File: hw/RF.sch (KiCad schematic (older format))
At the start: 18 parts

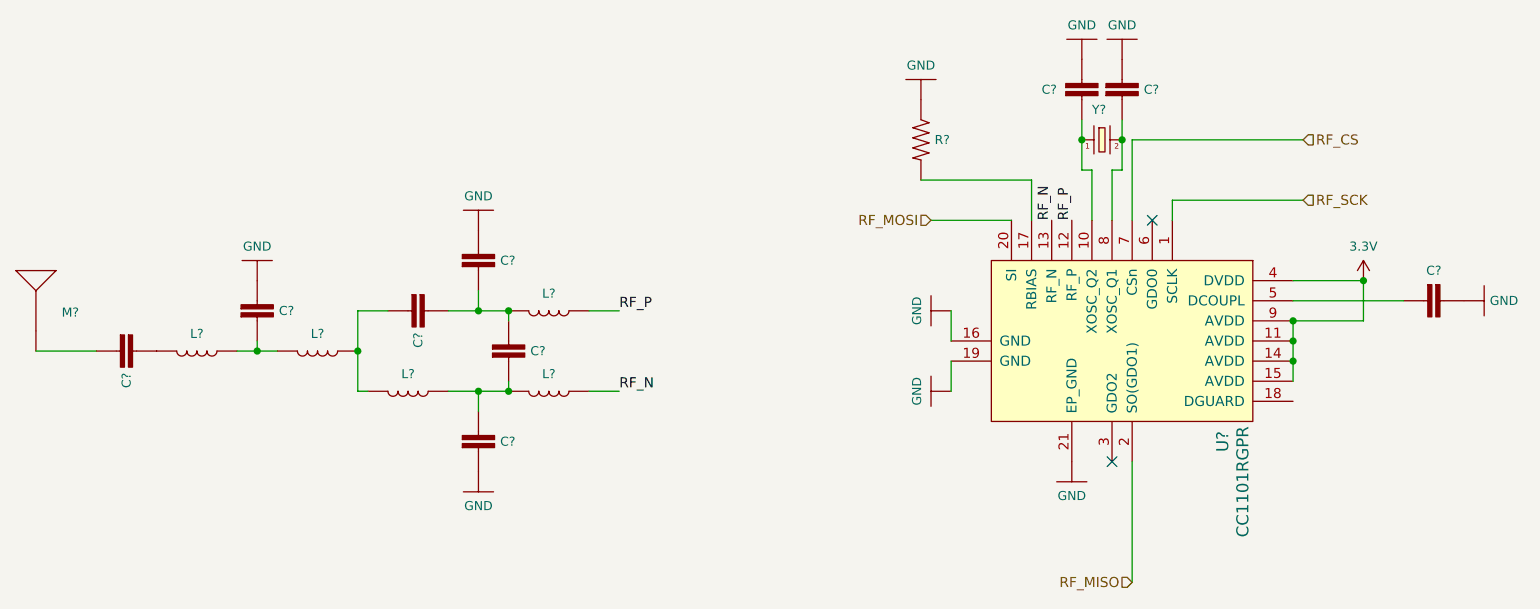
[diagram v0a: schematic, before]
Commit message: Create first revision of IMU sheet assign some footprints.
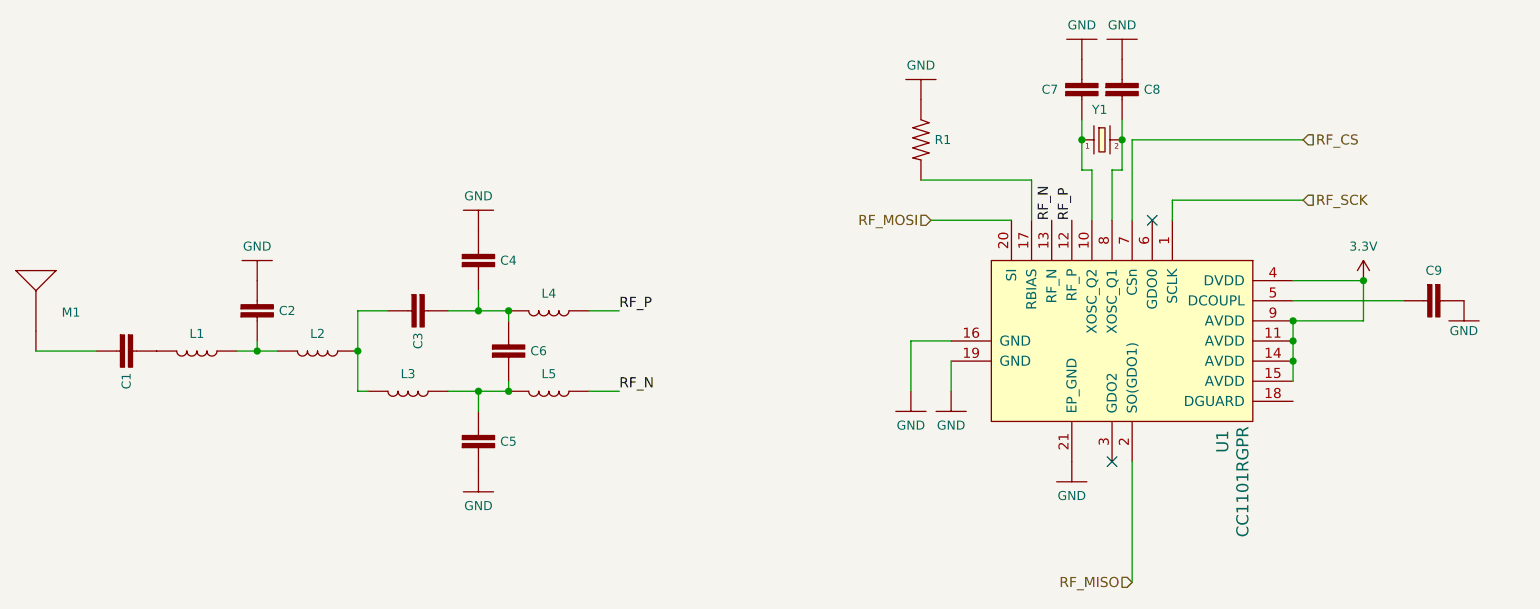
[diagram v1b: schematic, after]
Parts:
- gave numbers to parts that had none: 18
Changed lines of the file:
@@
 EESchema Schematic File Version 4
+LIBS:drone-cache
 EELAYER 30 0
 EELAYER END
 $Descr A 11000 8500
 encoding utf-8
-Sheet 2 2
+Sheet 2 3
 Title ""
 Date "2019-10-03"
@@
 $EndDescr
 $Comp
-L dk_RF-Transceiver-ICs:CC1101RGPR U?
+L dk_RF-Transceiver-ICs:CC1101RGPR U1
 U 1 1 5D96A68A
 P 7300 4000
-F 0 "U?" H 7800 4350 60  0000 C CNN
+F 0 "U1" H 7800 4350 60  0000 C CNN
 F 1 "CC1101RGPR" H 8000 4450 60  0000 C CNN
 F 2 "digikey-footprints:QFN-20-1EP_4x4mm_RevA" H 7500 4200 60  0001 L CNN
@@
 $EndComp
 $Comp
-L SparkFun-PowerSymbols:GND #GND?
+L SparkFun-PowerSymbols:GND #GND0101
 U 1 1 5D96E54E
 P 6300 4250
-F 0 "#GND?" H 6350 4200 45  0001 L BNN
+F 0 "#GND0101" H 6350 4200 45  0001 L BNN
 F 1 "GND" H 6300 4080 45  0000 C CNN
 F 2 "" H 6300 4150 60  0001 C CNN
 F 3 "" H 6300 4150 60  0001 C CNN
 	1    6300 4250
-	0    1    1    0
-$EndComp
-$Comp
-L SparkFun-PowerSymbols:GND #GND?
+	1    0    0    -1
+$EndComp
+$Comp
+L SparkFun-PowerSymbols:GND #GND0102
 U 1 1 5D96EA50
-P 6300 3850
-F 0 "#GND?" H 6350 3800 45  0001 L BNN
-F 1 "GND" H 6300 3680 45  0000 C CNN
-F 2 "" H 6300 3750 60  0001 C CNN
-F 3 "" H 6300 3750 60  0001 C CNN
-	1    6300 3850
-	0    1    1    0
+P 6100 4250
+F 0 "#GND0102" H 6150 4200 45  0001 L BNN
+F 1 "GND" H 6100 4080 45  0000 C CNN
+F 2 "" H 6100 4150 60  0001 C CNN
+F 3 "" H 6100 4150 60  0001 C CNN
+	1    6100 4250
+	1    0    0    -1
 $EndComp
 Wire Wire Line
 	6300 4100 6300 4250
-Wire Wire Line
-	6300 3850 6300 4000
-$Comp
-L SparkFun-Clocks:CRYSTALPTH-2X6 Y?
+$Comp
+L SparkFun-Clocks:CRYSTALPTH-2X6 Y1
 U 1 1 5D9752D5
 P 7050 3000
-F 0 "Y?" H 7000 3150 45  0000 L CNN
+F 0 "Y1" H 7000 3150 45  0000 L CNN
 F 1 "CRYSTALPTH-2X6" V 7050 2200 45  0001 L CNN
 F 2 "CRYSTAL-PTH-2X6-CYL" H 7050 3200 20  0001 C CNN
@@
 $EndComp
 $Comp
-L SparkFun-Capacitors:0.1UF-KIT-EZ-50V-20% C?
+L SparkFun-Capacitors:0.1UF-KIT-EZ-50V-20% C7
 U 1 1 5D981962
 P 6950 2800
-F 0 "C?" H 6750 2850 45  0000 L CNN
+F 0 "C7" H 6750 2850 45  0000 L CNN
 F 1 "0.1UF-KIT-EZ-50V-20%" H 7058 2861 45  0001 L CNN
 F 2 "CAP-PTH-SMALL-KIT" H 6950 3050 20  0001 C CNN
@@
 $EndComp
 $Comp
-L SparkFun-PowerSymbols:GND #GND?
+L SparkFun-PowerSymbols:GND #GND0103
 U 1 1 5D9935AD
 P 6950 2600
-F 0 "#GND?" H 7000 2550 45  0001 L BNN
+F 0 "#GND0103" H 7000 2550 45  0001 L BNN
 F 1 "GND" H 6950 2430 45  0000 C CNN
 F 2 "" H 6950 2500 60  0001 C CNN
@@
 Connection ~ 6950 3000
 $Comp
-L SparkFun-Capacitors:0.1UF-KIT-EZ-50V-20% C?
+L SparkFun-Capacitors:0.1UF-KIT-EZ-50V-20% C8
 U 1 1 5D9AA820
 P 7150 2800
-F 0 "C?" H 7258 2850 45  0000 L CNN
+F 0 "C8" H 7258 2850 45  0000 L CNN
 F 1 "0.1UF-KIT-EZ-50V-20%" H 7258 2861 45  0001 L CNN
 F 2 "CAP-PTH-SMALL-KIT" H 7150 3050 20  0001 C CNN
@@
 $EndComp
 $Comp
-L SparkFun-PowerSymbols:GND #GND?
+L SparkFun-PowerSymbols:GND #GND0104
 U 1 1 5D9AA826
 P 7150 2600
-F 0 "#GND?" H 7200 2550 45  0001 L BNN
+F 0 "#GND0104" H 7200 2550 45  0001 L BNN
 F 1 "GND" H 7150 2430 45  0000 C CNN
 F 2 "" H 7150 2500 60  0001 C CNN
@@
 Connection ~ 8000 4100
 $Comp
-L SparkFun-PowerSymbols:3.3V #SUPPLY?
+L SparkFun-PowerSymbols:3.3V #SUPPLY0101
 U 1 1 5D9B151B
 P 8350 3700
-F 0 "#SUPPLY?" H 8400 3700 45  0001 L BNN
+F 0 "#SUPPLY0101" H 8400 3700 45  0001 L BNN
 F 1 "3.3V" H 8350 3870 45  0000 C CNN
 F 2 "XXX-00000" H 8350 3881 60  0001 C CNN
@@
 RF_SCK
 $Comp
-L SparkFun-PowerSymbols:GND #GND?
+L SparkFun-PowerSymbols:GND #GND0105
 U 1 1 5D9B86E3
 P 6150 2800
-F 0 "#GND?" H 6200 2750 45  0001 L BNN
+F 0 "#GND0105" H 6200 2750 45  0001 L BNN
 F 1 "GND" H 6150 2630 45  0000 C CNN
 F 2 "" H 6150 2700 60  0001 C CNN
@@
 $EndComp
 $Comp
-L SparkFun-Resistors:RESISTOR0402 R?
+L SparkFun-Resistors:RESISTOR0402 R1
 U 1 1 5D9B8F7F
 P 6150 3000
-F 0 "R?" V 6150 3068 45  0000 L CNN
+F 0 "R1" V 6150 3068 45  0000 L CNN
 F 1 "RESISTOR0402" V 6139 3068 45  0001 L CNN
 F 2 "0402" H 6150 3150 20  0001 C CNN
@@
 	7200 4600 7200 5200
 $Comp
-L SparkFun-PowerSymbols:GND #GND?
+L SparkFun-PowerSymbols:GND #GND0106
 U 1 1 5D9F85B8
 P 6900 4600
-F 0 "#GND?" H 6950 4550 45  0001 L BNN
+F 0 "#GND0106" H 6950 4550 45  0001 L BNN
 F 1 "GND" H 6900 4430 45  0000 C CNN
 F 2 "" H 6900 4500 60  0001 C CNN
@@
 $EndComp
 $Comp
-L SparkFun-Capacitors:0.1UF-KIT-EZ-50V-20% C?
+L SparkFun-Capacitors:0.1UF-KIT-EZ-50V-20% C9
 U 1 1 5DA0075A
 P 8650 3800
-F 0 "C?" V 8500 3850 45  0000 C CNN
+F 0 "C9" V 8500 3850 45  0000 C CNN
 F 1 "0.1UF-KIT-EZ-50V-20%" H 8758 3861 45  0001 L CNN
 F 2 "CAP-PTH-SMALL-KIT" H 8650 4050 20  0001 C CNN
@@
 	8000 3800 8550 3800
 $Comp
-L SparkFun-PowerSymbols:GND #GND?
+L SparkFun-PowerSymbols:GND #GND0107
 U 1 1 5DA01234
 P 8850 3800
-F 0 "#GND?" H 8900 3750 45  0001 L BNN
-F 1 "GND" V 8850 3672 45  0000 R CNN
+F 0 "#GND0107" H 8900 3750 45  0001 L BNN
+F 1 "GND" H 8920 3650 45  0000 R CNN
 F 2 "" H 8850 3700 60  0001 C CNN
 F 3 "" H 8850 3700 60  0001 C CNN
 	1    8850 3800
-	0    -1   -1   0
+	1    0    0    -1
 $EndComp
 Text Label 6800 3400 1    50   ~ 0
@@
 RF_P
 $Comp
-L SparkFun-Coils:INDUCTOR-0402-3.9NH L?
+L SparkFun-Coils:INDUCTOR-0402-3.9NH L5
 U 1 1 5DA164EE
 P 4300 4250
-F 0 "L?" V 4214 4250 45  0000 C CNN
+F 0 "L5" V 4214 4250 45  0000 C CNN
 F 1 "INDUCTOR-0402-3.9NH" V 4108 4250 45  0001 C CNN
 F 2 "0402" H 4300 4500 20  0001 C CNN
@@
 $EndComp
 $Comp
-L SparkFun-Coils:INDUCTOR-0402-3.9NH L?
+L SparkFun-Coils:INDUCTOR-0402-3.9NH L4
 U 1 1 5DA177FA
 P 4300 3850
-F 0 "L?" V 4214 3850 45  0000 C CNN
+F 0 "L4" V 4214 3850 45  0000 C CNN
 F 1 "INDUCTOR-0402-3.9NH" V 4108 3850 45  0001 C CNN
 F 2 "0402" H 4300 4100 20  0001 C CNN
@@
 $EndComp
 $Comp
-L SparkFun-Coils:INDUCTOR-0402-3.9NH L?
+L SparkFun-Coils:INDUCTOR-0402-3.9NH L3
 U 1 1 5DA17EF8
 P 3600 4250
-F 0 "L?" V 3514 4250 45  0000 C CNN
+F 0 "L3" V 3514 4250 45  0000 C CNN
 F 1 "INDUCTOR-0402-3.9NH" V 3408 4250 45  0001 C CNN
 F 2 "0402" H 3600 4500 20  0001 C CNN
@@
 $EndComp
 $Comp
-L SparkFun-Capacitors:0.1UF-KIT-EZ-50V-20% C?
+L SparkFun-Capacitors:0.1UF-KIT-EZ-50V-20% C6
 U 1 1 5DA1B017
 P 4100 4100
-F 0 "C?" H 4208 4150 45  0000 L CNN
+F 0 "C6" H 4208 4150 45  0000 L CNN
 F 1 "0.1UF-KIT-EZ-50V-20%" H 4208 4161 45  0001 L CNN
 F 2 "CAP-PTH-SMALL-KIT" H 4100 4350 20  0001 C CNN
@@
 $EndComp
 $Comp
-L SparkFun-Capacitors:0.1UF-KIT-EZ-50V-20% C?
+L SparkFun-Capacitors:0.1UF-KIT-EZ-50V-20% C3
 U 1 1 5DA1BF75
 P 3600 3850
-F 0 "C?" H 3708 3900 45  0000 L CNN
+F 0 "C3" H 3708 3900 45  0000 L CNN
 F 1 "0.1UF-KIT-EZ-50V-20%" H 3708 3911 45  0001 L CNN
 F 2 "CAP-PTH-SMALL-KIT" H 3600 4100 20  0001 C CNN
@@
 $EndComp
 $Comp
-L SparkFun-Capacitors:0.1UF-KIT-EZ-50V-20% C?
+L SparkFun-Capacitors:0.1UF-KIT-EZ-50V-20% C4
 U 1 1 5DA21E27
 P 3950 3650
-F 0 "C?" H 4058 3700 45  0000 L CNN
+F 0 "C4" H 4058 3700 45  0000 L CNN
 F 1 "0.1UF-KIT-EZ-50V-20%" H 4058 3711 45  0001 L CNN
 F 2 "CAP-PTH-SMALL-KIT" H 3950 3900 20  0001 C CNN
@@
 $EndComp
 $Comp
-L SparkFun-Capacitors:0.1UF-KIT-EZ-50V-20% C?
+L SparkFun-Capacitors:0.1UF-KIT-EZ-50V-20% C5
 U 1 1 5DA225FB
 P 3950 4550
-F 0 "C?" H 4058 4600 45  0000 L CNN
+F 0 "C5" H 4058 4600 45  0000 L CNN
 F 1 "0.1UF-KIT-EZ-50V-20%" H 4058 4611 45  0001 L CNN
 F 2 "CAP-PTH-SMALL-KIT" H 3950 4800 20  0001 C CNN
@@
 $EndComp
 $Comp
-L SparkFun-PowerSymbols:GND #GND?
+L SparkFun-PowerSymbols:GND #GND0108
 U 1 1 5DA26B2C
 P 3950 3450
-F 0 "#GND?" H 4000 3400 45  0001 L BNN
+F 0 "#GND0108" H 4000 3400 45  0001 L BNN
 F 1 "GND" H 3950 3280 45  0000 C CNN
 F 2 "" H 3950 3350 60  0001 C CNN
@@
 $EndComp
 $Comp
-L SparkFun-PowerSymbols:GND #GND?
+L SparkFun-PowerSymbols:GND #GND0109
 U 1 1 5DA2723A
 P 3950 4650
-F 0 "#GND?" H 4000 4600 45  0001 L BNN
+F 0 "#GND0109" H 4000 4600 45  0001 L BNN
 F 1 "GND" H 3950 4480 45  0000 C CNN
 F 2 "" H 3950 4550 60  0001 C CNN
@@
 	3950 3850 4100 3850
 $Comp
-L SparkFun-Capacitors:0.1UF-KIT-EZ-50V-20% C?
+L SparkFun-Capacitors:0.1UF-KIT-EZ-50V-20% C2
 U 1 1 5DA59F11
 P 2850 3900
-F 0 "C?" H 2958 3950 45  0000 L CNN
+F 0 "C2" H 2958 3950 45  0000 L CNN
 F 1 "0.1UF-KIT-EZ-50V-20%" H 2958 3961 45  0001 L CNN
 F 2 "CAP-PTH-SMALL-KIT" H 2850 4150 20  0001 C CNN
@@
 $EndComp
 $Comp
-L SparkFun-PowerSymbols:GND #GND?
+L SparkFun-PowerSymbols:GND #GND0110
 U 1 1 5DA59F17
 P 2850 3700
-F 0 "#GND?" H 2900 3650 45  0001 L BNN
+F 0 "#GND0110" H 2900 3650 45  0001 L BNN
 F 1 "GND" H 2850 3530 45  0000 C CNN
 F 2 "" H 2850 3600 60  0001 C CNN
@@
 $EndComp
 $Comp
-L SparkFun-Coils:INDUCTOR-0402-3.9NH L?
+L SparkFun-Coils:INDUCTOR-0402-3.9NH L2
 U 1 1 5DA5E843
 P 3150 4050
-F 0 "L?" V 3064 4050 45  0000 C CNN
+F 0 "L2" V 3064 4050 45  0000 C CNN
 F 1 "INDUCTOR-0402-3.9NH" V 2958 4050 45  0001 C CNN
 F 2 "0402" H 3150 4300 20  0001 C CNN
@@
 	2850 4050 2850 4000
 $Comp
-L SparkFun-Coils:INDUCTOR-0402-3.9NH L?
+L SparkFun-Coils:INDUCTOR-0402-3.9NH L1
 U 1 1 5DA62FAF
 P 2550 4050
-F 0 "L?" V 2464 4050 45  0000 C CNN
+F 0 "L1" V 2464 4050 45  0000 C CNN
 F 1 "INDUCTOR-0402-3.9NH" V 2358 4050 45  0001 C CNN
 F 2 "0402" H 2550 4300 20  0001 C CNN
@@
 Connection ~ 2850 4050
 $Comp
-L SparkFun-Capacitors:0.1UF-KIT-EZ-50V-20% C?
+L SparkFun-Capacitors:0.1UF-KIT-EZ-50V-20% C1
 U 1 1 5DA65A2E
 P 2150 4050
-F 0 "C?" H 2258 4100 45  0000 L CNN
+F 0 "C1" H 2258 4100 45  0000 L CNN
 F 1 "0.1UF-KIT-EZ-50V-20%" H 2258 4111 45  0001 L CNN
 F 2 "CAP-PTH-SMALL-KIT" H 2150 4300 20  0001 C CNN
@@
 $EndComp
 $Comp
-L SparkFun-GPS:ANTENNAGPS-2X7MM M?
+L SparkFun-GPS:ANTENNAGPS-2X7MM M1
 U 1 1 5DA673F3
 P 1750 3850
-F 0 "M?" H 1878 3842 45  0000 L CNN
+F 0 "M1" H 1878 3842 45  0000 L CNN
 F 1 "ANTENNAGPS-2X7MM" H 1878 3853 45  0001 L CNN
 F 2 "ANT-GPS-2X7MM" H 1750 4100 20  0001 C CNN
@@
 Wire Wire Line
 	2050 4050 1750 4050
+Wire Wire Line
+	6300 4000 6100 4000
+Wire Wire Line
+	6100 4000 6100 4250
 $EndSCHEMATC

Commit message: Add valid footprints to most schematic symbols. Add pin headers.
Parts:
- C1, C2, C3, C4, C5, C6, C7, C8, C9: footprint CAP-PTH-SMALL-KIT -> Capacitor_SMD:C_0603_1608Metric
- L1, L2, L3, L4, L5: footprint 0402 -> Inductor_SMD:L_0805_2012Metric
- M1: footprint ANT-GPS-2X7MM -> TestPoint:TestPoint_2Pads_Pitch2.54mm_Drill0.8mm
- R1: footprint 0402 -> Resistor_SMD:R_0603_1608Metric
- U1: footprint digikey-footprints:QFN-20-1EP_4x4mm_RevA -> Package_DFN_QFN:QFN-20-1EP_4x4mm_P0.5mm_EP2.7x2.7mm_ThermalVias
- Y1: footprint CRYSTAL-PTH-2X6-CYL -> Crystal:Crystal_AT310_D3.0mm_L10.0mm_Horizontal
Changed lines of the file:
@@
 F 0 "U1" H 7800 4350 60  0000 C CNN
 F 1 "CC1101RGPR" H 8000 4450 60  0000 C CNN
-F 2 "digikey-footprints:QFN-20-1EP_4x4mm_RevA" H 7500 4200 60  0001 L CNN
+F 2 "Package_DFN_QFN:QFN-20-1EP_4x4mm_P0.5mm_EP2.7x2.7mm_ThermalVias" H 7500 4200 60  0001 L CNN
 F 3 "http://www.ti.com/general/docs/suppproductinfo.tsp?distId=10&gotoUrl=http%3A%2F%2Fwww.ti.com%2Flit%2Fgpn%2Fcc1101" H 7500 4300 60  0001 L CNN
 F 4 "296-35718-1-ND" H 7500 4400 60  0001 L CNN "Digi-Key_PN"
@@
 F 0 "Y1" H 7000 3150 45  0000 L CNN
 F 1 "CRYSTALPTH-2X6" V 7050 2200 45  0001 L CNN
-F 2 "CRYSTAL-PTH-2X6-CYL" H 7050 3200 20  0001 C CNN
+F 2 "Crystal:Crystal_AT310_D3.0mm_L10.0mm_Horizontal" H 7050 3200 20  0001 C CNN
 F 3 "" H 7050 3000 50  0001 C CNN
 F 4 "XXX-00000" V 7150 2250 60  0001 L CNN "Field4"
@@
 F 0 "C7" H 6750 2850 45  0000 L CNN
 F 1 "0.1UF-KIT-EZ-50V-20%" H 7058 2861 45  0001 L CNN
-F 2 "CAP-PTH-SMALL-KIT" H 6950 3050 20  0001 C CNN
+F 2 "Capacitor_SMD:C_0603_1608Metric" H 6950 3050 20  0001 C CNN
 F 3 "" H 6950 2800 50  0001 C CNN
 F 4 "CAP-08370" H 7058 2766 60  0001 L CNN "Field4"
@@
 F 0 "C8" H 7258 2850 45  0000 L CNN
 F 1 "0.1UF-KIT-EZ-50V-20%" H 7258 2861 45  0001 L CNN
-F 2 "CAP-PTH-SMALL-KIT" H 7150 3050 20  0001 C CNN
+F 2 "Capacitor_SMD:C_0603_1608Metric" H 7150 3050 20  0001 C CNN
 F 3 "" H 7150 2800 50  0001 C CNN
 F 4 "CAP-08370" H 7258 2766 60  0001 L CNN "Field4"
@@
 F 0 "R1" V 6150 3068 45  0000 L CNN
 F 1 "RESISTOR0402" V 6139 3068 45  0001 L CNN
-F 2 "0402" H 6150 3150 20  0001 C CNN
+F 2 "Resistor_SMD:R_0603_1608Metric" H 6150 3150 20  0001 C CNN
 F 3 "" H 6150 3000 60  0001 C CNN
 F 4 " " V 6234 3068 60  0001 L CNN "Field4"
@@
 F 0 "C9" V 8500 3850 45  0000 C CNN
 F 1 "0.1UF-KIT-EZ-50V-20%" H 8758 3861 45  0001 L CNN
-F 2 "CAP-PTH-SMALL-KIT" H 8650 4050 20  0001 C CNN
+F 2 "Capacitor_SMD:C_0603_1608Metric" H 8650 4050 20  0001 C CNN
 F 3 "" H 8650 3800 50  0001 C CNN
 F 4 "CAP-08370" H 8758 3766 60  0001 L CNN "Field4"
@@
 F 0 "L5" V 4214 4250 45  0000 C CNN
 F 1 "INDUCTOR-0402-3.9NH" V 4108 4250 45  0001 C CNN
-F 2 "0402" H 4300 4500 20  0001 C CNN
+F 2 "Inductor_SMD:L_0805_2012Metric" H 4300 4500 20  0001 C CNN
 F 3 "" H 4300 4250 50  0001 C CNN
 F 4 "NDUC-13457" V 4203 4250 60  0001 C CNN "Field4"
@@
 F 0 "L4" V 4214 3850 45  0000 C CNN
 F 1 "INDUCTOR-0402-3.9NH" V 4108 3850 45  0001 C CNN
-F 2 "0402" H 4300 4100 20  0001 C CNN
+F 2 "Inductor_SMD:L_0805_2012Metric" H 4300 4100 20  0001 C CNN
 F 3 "" H 4300 3850 50  0001 C CNN
 F 4 "NDUC-13457" V 4203 3850 60  0001 C CNN "Field4"
@@
 F 0 "L3" V 3514 4250 45  0000 C CNN
 F 1 "INDUCTOR-0402-3.9NH" V 3408 4250 45  0001 C CNN
-F 2 "0402" H 3600 4500 20  0001 C CNN
+F 2 "Inductor_SMD:L_0805_2012Metric" H 3600 4500 20  0001 C CNN
 F 3 "" H 3600 4250 50  0001 C CNN
 F 4 "NDUC-13457" V 3503 4250 60  0001 C CNN "Field4"
@@
 F 0 "C6" H 4208 4150 45  0000 L CNN
 F 1 "0.1UF-KIT-EZ-50V-20%" H 4208 4161 45  0001 L CNN
-F 2 "CAP-PTH-SMALL-KIT" H 4100 4350 20  0001 C CNN
+F 2 "Capacitor_SMD:C_0603_1608Metric" H 4100 4350 20  0001 C CNN
 F 3 "" H 4100 4100 50  0001 C CNN
 F 4 "CAP-08370" H 4208 4066 60  0001 L CNN "Field4"
@@
 F 0 "C3" H 3708 3900 45  0000 L CNN
 F 1 "0.1UF-KIT-EZ-50V-20%" H 3708 3911 45  0001 L CNN
-F 2 "CAP-PTH-SMALL-KIT" H 3600 4100 20  0001 C CNN
+F 2 "Capacitor_SMD:C_0603_1608Metric" H 3600 4100 20  0001 C CNN
 F 3 "" H 3600 3850 50  0001 C CNN
 F 4 "CAP-08370" H 3708 3816 60  0001 L CNN "Field4"
@@
 F 0 "C4" H 4058 3700 45  0000 L CNN
 F 1 "0.1UF-KIT-EZ-50V-20%" H 4058 3711 45  0001 L CNN
-F 2 "CAP-PTH-SMALL-KIT" H 3950 3900 20  0001 C CNN
+F 2 "Capacitor_SMD:C_0603_1608Metric" H 3950 3900 20  0001 C CNN
 F 3 "" H 3950 3650 50  0001 C CNN
 F 4 "CAP-08370" H 4058 3616 60  0001 L CNN "Field4"
@@
 F 0 "C5" H 4058 4600 45  0000 L CNN
 F 1 "0.1UF-KIT-EZ-50V-20%" H 4058 4611 45  0001 L CNN
-F 2 "CAP-PTH-SMALL-KIT" H 3950 4800 20  0001 C CNN
+F 2 "Capacitor_SMD:C_0603_1608Metric" H 3950 4800 20  0001 C CNN
 F 3 "" H 3950 4550 50  0001 C CNN
 F 4 "CAP-08370" H 4058 4516 60  0001 L CNN "Field4"
@@
 F 0 "C2" H 2958 3950 45  0000 L CNN
 F 1 "0.1UF-KIT-EZ-50V-20%" H 2958 3961 45  0001 L CNN
-F 2 "CAP-PTH-SMALL-KIT" H 2850 4150 20  0001 C CNN
+F 2 "Capacitor_SMD:C_0603_1608Metric" H 2850 4150 20  0001 C CNN
 F 3 "" H 2850 3900 50  0001 C CNN
 F 4 "CAP-08370" H 2958 3866 60  0001 L CNN "Field4"
@@
 F 0 "L2" V 3064 4050 45  0000 C CNN
 F 1 "INDUCTOR-0402-3.9NH" V 2958 4050 45  0001 C CNN
-F 2 "0402" H 3150 4300 20  0001 C CNN
+F 2 "Inductor_SMD:L_0805_2012Metric" H 3150 4300 20  0001 C CNN
 F 3 "" H 3150 4050 50  0001 C CNN
 F 4 "NDUC-13457" V 3053 4050 60  0001 C CNN "Field4"
@@
 F 0 "L1" V 2464 4050 45  0000 C CNN
 F 1 "INDUCTOR-0402-3.9NH" V 2358 4050 45  0001 C CNN
-F 2 "0402" H 2550 4300 20  0001 C CNN
+F 2 "Inductor_SMD:L_0805_2012Metric" H 2550 4300 20  0001 C CNN
 F 3 "" H 2550 4050 50  0001 C CNN
 F 4 "NDUC-13457" V 2453 4050 60  0001 C CNN "Field4"
@@
 F 0 "C1" H 2258 4100 45  0000 L CNN
 F 1 "0.1UF-KIT-EZ-50V-20%" H 2258 4111 45  0001 L CNN
-F 2 "CAP-PTH-SMALL-KIT" H 2150 4300 20  0001 C CNN
+F 2 "Capacitor_SMD:C_0603_1608Metric" H 2150 4300 20  0001 C CNN
 F 3 "" H 2150 4050 50  0001 C CNN
 F 4 "CAP-08370" H 2258 4016 60  0001 L CNN "Field4"
@@
 F 0 "M1" H 1878 3842 45  0000 L CNN
 F 1 "ANTENNAGPS-2X7MM" H 1878 3853 45  0001 L CNN
-F 2 "ANT-GPS-2X7MM" H 1750 4100 20  0001 C CNN
+F 2 "TestPoint:TestPoint_2Pads_Pitch2.54mm_Drill0.8mm" H 1750 4100 20  0001 C CNN
 F 3 "" H 1750 3850 50  0001 C CNN
 F 4 "ANT-09087" H 1878 3758 60  0001 L CNN "Field4"
